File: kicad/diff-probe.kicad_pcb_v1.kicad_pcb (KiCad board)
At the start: 2 copper layers, 49.2 x 20.5 mm, 44 parts, among them J1 HEADER-1X2CARD-EDGE, J3 Molex 502494-0470, J4 901-10511-3, U1 OPA847xDBV, U2 OPA847xDBV, U3 AP3211K, U4 AP3211K

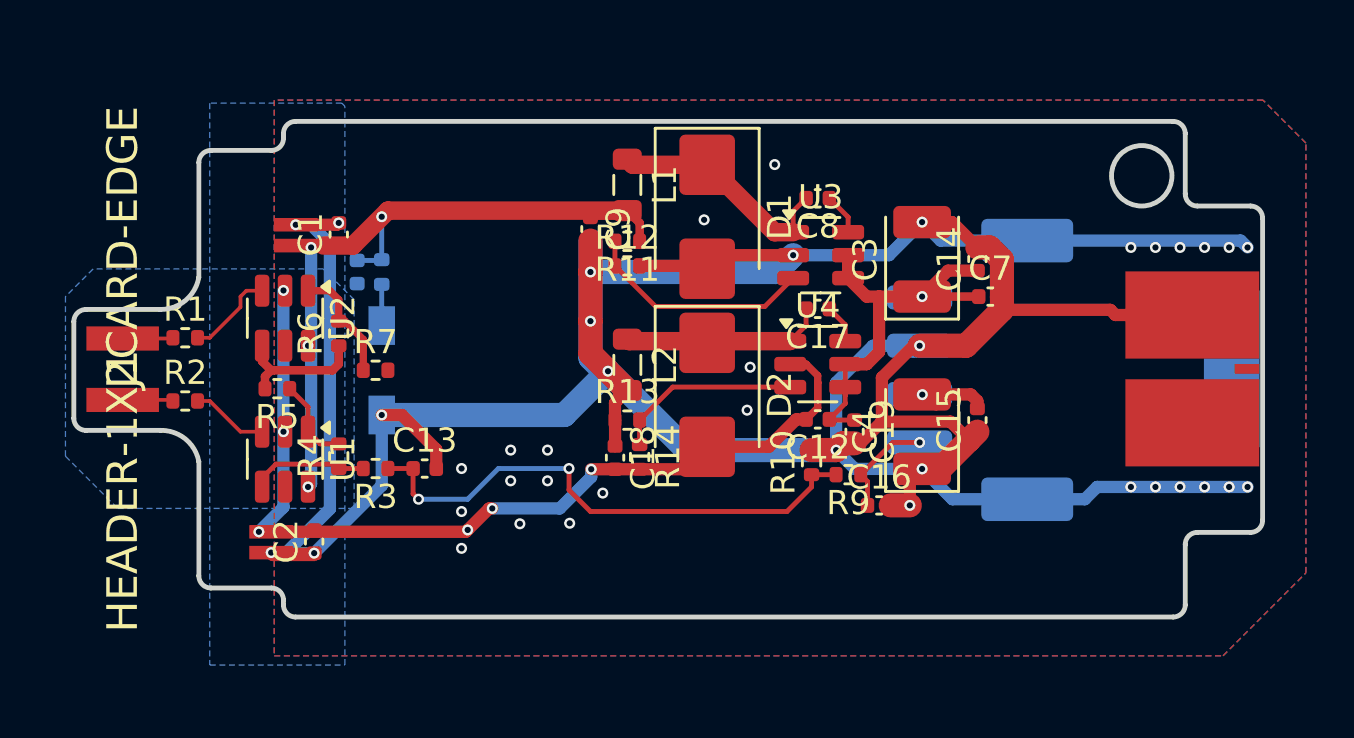
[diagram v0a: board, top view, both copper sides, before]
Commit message: Update project. Route signals, make a coplanar 50 R output - two layer board.
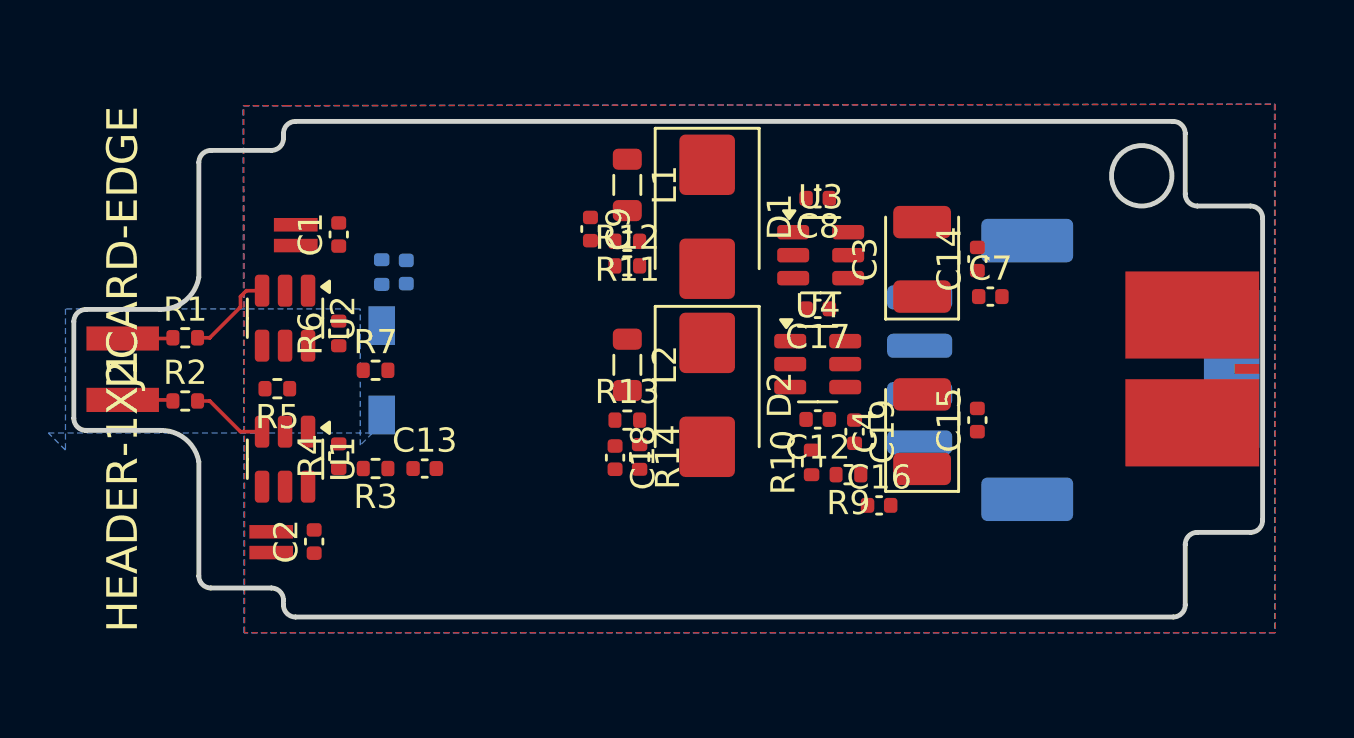
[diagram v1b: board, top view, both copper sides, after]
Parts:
- moved C10 2.03 mm to (138.4, 94.0)
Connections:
- C10 pad 1: /Power_supply/V+ -> Net-(C10-Pad1)
- J3 pad MP: GND -> (no net)
- R26 pad 2: /Power_supply/V+ -> Net-(C10-Pad1)
- U1 pad 2: /Power_supply/V- -> Net-(U1-V-)
- U1 pad 6: /Power_supply/V+ -> Net-(U1-V+)
- U2 pad 2: /Power_supply/V- -> Net-(U2-V-)
- U2 pad 6: /Power_supply/V+ -> Net-(U2-V+)
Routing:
- net GND: track 162.9 -> 0.00 mm, vias 40 -> 0
- net /Power_supply/V-: track 55.0 -> 0.00 mm, vias 6 -> 0
- net /OutPad: track 45.9 -> 0.00 mm
- net /Power_supply/V+: track 41.0 -> 0.00 mm, vias 4 -> 0
- net /offset_prec: track 22.4 -> 0.00 mm, vias 2 -> 0
- net /Power_supply/IN_P: track 19.9 -> 0.00 mm, vias 1 -> 0
- net Net-(D2-K): track 11.9 -> 0.00 mm
- net Net-(D1-K): track 9.73 -> 0.00 mm
- net Net-(U3-FB): track 9.57 -> 0.00 mm
- net Net-(U4-FB): track 7.81 -> 0.00 mm
- net Net-(U2--): track 5.70 -> 0.00 mm
- net /OUT: track 4.92 -> 0.00 mm
- net Net-(U1--): track 4.86 -> 0.00 mm
- net /offset: track 4.37 -> 0.00 mm, vias 1 -> 0
- net Net-(R4-Pad2): track 3.57 -> 0.00 mm
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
